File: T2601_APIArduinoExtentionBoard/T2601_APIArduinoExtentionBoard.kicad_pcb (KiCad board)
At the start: 4 copper layers, 59.8 x 90 mm, 100 parts, among them J1 Conn_01x10_Socket, J10 Conn_02x03_Counter_Clockwise, J11 Conn_01x04, J12 Screw_Terminal_01x02, J14 Screw_Terminal_01x02, J2 Conn_01x10_Socket, J20 Conn_02x08_Counter_Clockwise, J21 Conn_02x08_Counter_Clockwise, J3 Conn_01x10_Socket, J30 Conn_01x04_Pin, J31 Conn_01x04_Pin, J4 Conn_01x10_Socket, J5 Screw_Terminal_01x08, J6 Screw_Terminal_01x08, U2 ATmega328PB-A, X1 X322516MOB4SI

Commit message: Reorganisation schematic
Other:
- board text added: "T2601 APIArduino V1.0 Extention JGY & DDP"
- board text removed: "T2601 APIArduino V1 Extention JGY & DDP"
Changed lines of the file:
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@@
 		)
 	)
-	(gr_text "T2601 APIArduino\nV1 Extention\nJGY & DDP"
+	(gr_text "T2601 APIArduino\nV1.0 Extention\nJGY & DDP"
 		(at 153.434 105.534 0)
 		(layer "F.SilkS")
@@
 	)
 	(segment
+		(start 129.6416 114.4778)
+		(end 129.6416 109.6264)
+		(width 1)
+		(layer "F.Cu")
+		(net "Net-(J4-Pin_10)")
+	)
+	(segment
+		(start 129.6416 109.6264)
+		(end 130.81 108.458)
+		(width 1)
+		(layer "F.Cu")
+		(net "Net-(J4-Pin_10)")
+	)
+	(segment
+		(start 132.1816 109.6264)
+		(end 133.35 108.458)
+		(width 1)
+		(layer "F.Cu")
+		(net "Net-(J4-Pin_9)")
+	)
+	(segment
+		(start 132.1816 114.4778)
+		(end 132.1816 109.6264)
+		(width 1)
+		(layer "F.Cu")
+		(net "Net-(J4-Pin_9)")
+	)
+	(segment
+		(start 134.7216 109.626399)
+		(end 135.889999 108.458)
+		(width 1)
+		(layer "F.Cu")
+		(net "Net-(J4-Pin_8)")
+	)
+	(segment
+		(start 134.7216 114.4778)
+		(end 134.7216 109.626399)
+		(width 1)
+		(layer "F.Cu")
+		(net "Net-(J4-Pin_8)")
+	)
+	(segment
+		(start 137.2616 114.4778)
+		(end 137.2616 109.6264)
+		(width 1)
+		(layer "F.Cu")
+		(net "Net-(J4-Pin_7)")
+	)
+	(segment
+		(start 137.2616 109.6264)
+		(end 138.43 108.458)
+		(width 1)
+		(layer "F.Cu")
+		(net "Net-(J4-Pin_7)")
+	)
+	(segment
+		(start 146.05 108.458)
+		(end 145.796 108.458)
+		(width 1)
+		(layer "F.Cu")
+		(net "Net-(J4-Pin_4)")
+	)
+	(segment
+		(start 145.8214 108.458)
+		(end 146.05 108.458)
+		(width 1)
+		(layer "F.Cu")
+		(net "Net-(J4-Pin_4)")
+	)
+	(segment
+		(start 139.8016 114.4778)
+		(end 145.8214 108.458)
+		(width 1)
+		(layer "F.Cu")
+		(net "Net-(J4-Pin_4)")
+	)
+	(segment
+		(start 148.3614 108.458)
+		(end 148.590001 108.458)
+		(width 1)
+		(layer "F.Cu")
+		(net "Net-(J4-Pin_3)")
+	)
+	(segment
+		(start 148.590001 108.458)
+		(end 148.336 108.458)
+		(width 1)
+		(layer "F.Cu")
+		(net "Net-(J4-Pin_3)")
+	)
+	(segment
+		(start 142.3416 114.4778)
+		(end 148.3614 108.458)
+		(width 1)
+		(layer "F.Cu")
+		(net "Net-(J4-Pin_3)")
+	)
+	(segment
+		(start 151.13 108.458)
+		(end 150.876 108.458)
+		(width 1)
+		(layer "F.Cu")
+		(net "Net-(J4-Pin_2)")
+	)
+	(segment
+		(start 144.8816 114.4778)
+		(end 150.9014 108.458)
+		(width 1)
+		(layer "F.Cu")
+		(net "Net-(J4-Pin_2)")
+	)
+	(segment
+		(start 150.9014 108.458)
+		(end 151.13 108.458)
+		(width 1)
+		(layer "F.Cu")
+		(net "Net-(J4-Pin_2)")
+	)
+	(segment
+		(start 153.67 108.458)
+		(end 153.416 108.458)
+		(width 1)
+		(layer "F.Cu")
+		(net "Net-(J4-Pin_1)")
+	)
+	(segment
+		(start 147.4216 114.4778)
+		(end 147.6502 114.4778)
+		(width 1)
+		(layer "F.Cu")
+		(net "Net-(J4-Pin_1)")
+	)
+	(segment
+		(start 147.6502 114.4778)
+		(end 153.67 108.458)
+		(width 1)
+		(layer "F.Cu")
+		(net "Net-(J4-Pin_1)")
+	)
+	(segment
 		(start 130.7592 70.1256)
 		(end 135.36 65.5248)
@@
 		(net "Net-(D12-Pad1)")
 	)
-	(segment
-		(start 134.7216 109.626399)
-		(end 135.889999 108.458)
-		(width 1)
-		(layer "F.Cu")
-		(net "Net-(J4-Pin_8)")
-	)
-	(segment
-		(start 134.7216 114.4778)
-		(end 134.7216 109.626399)
-		(width 1)
-		(layer "F.Cu")
-		(net "Net-(J4-Pin_8)")
-	)
-	(segment
-		(start 129.6416 114.4778)
-		(end 129.6416 109.6264)
-		(width 1)
-		(layer "F.Cu")
-		(net "Net-(J4-Pin_10)")
-	)
-	(segment
-		(start 129.6416 109.6264)
-		(end 130.81 108.458)
-		(width 1)
-		(layer "F.Cu")
-		(net "Net-(J4-Pin_10)")
-	)
-	(segment
-		(start 146.05 108.458)
-		(end 145.796 108.458)
-		(width 1)
-		(layer "F.Cu")
-		(net "Net-(J4-Pin_4)")
-	)
-	(segment
-		(start 145.8214 108.458)
-		(end 146.05 108.458)
-		(width 1)
-		(layer "F.Cu")
-		(net "Net-(J4-Pin_4)")
-	)
-	(segment
-		(start 139.8016 114.4778)
-		(end 145.8214 108.458)
-		(width 1)
-		(layer "F.Cu")
-		(net "Net-(J4-Pin_4)")
-	)
-	(segment
-		(start 151.13 108.458)
-		(end 150.876 108.458)
-		(width 1)
-		(layer "F.Cu")
-		(net "Net-(J4-Pin_2)")
-	)
-	(segment
-		(start 144.8816 114.4778)
-		(end 150.9014 108.458)
-		(width 1)
-		(layer "F.Cu")
-		(net "Net-(J4-Pin_2)")
-	)
-	(segment
-		(start 150.9014 108.458)
-		(end 151.13 108.458)
-		(width 1)
-		(layer "F.Cu")
-		(net "Net-(J4-Pin_2)")
-	)
-	(segment
-		(start 137.2616 114.4778)
-		(end 137.2616 109.6264)
-		(width 1)
-		(layer "F.Cu")
-		(net "Net-(J4-Pin_7)")
-	)
-	(segment
-		(start 137.2616 109.6264)
-		(end 138.43 108.458)
-		(width 1)
-		(layer "F.Cu")
-		(net "Net-(J4-Pin_7)")
-	)
-	(segment
-		(start 148.3614 108.458)
-		(end 148.590001 108.458)
-		(width 1)
-		(layer "F.Cu")
-		(net "Net-(J4-Pin_3)")
-	)
-	(segment
-		(start 148.590001 108.458)
-		(end 148.336 108.458)
-		(width 1)
-		(layer "F.Cu")
-		(net "Net-(J4-Pin_3)")
-	)
-	(segment
-		(start 142.3416 114.4778)
-		(end 148.3614 108.458)
-		(width 1)
-		(layer "F.Cu")
-		(net "Net-(J4-Pin_3)")
-	)
-	(segment
-		(start 132.1816 109.6264)
-		(end 133.35 108.458)
-		(width 1)
-		(layer "F.Cu")
-		(net "Net-(J4-Pin_9)")
-	)
-	(segment
-		(start 132.1816 114.4778)
-		(end 132.1816 109.6264)
-		(width 1)
-		(layer "F.Cu")
-		(net "Net-(J4-Pin_9)")
-	)
-	(segment
-		(start 153.67 108.458)
-		(end 153.416 108.458)
-		(width 1)
-		(layer "F.Cu")
-		(net "Net-(J4-Pin_1)")
-	)
-	(segment
-		(start 147.4216 114.4778)
-		(end 147.6502 114.4778)
-		(width 1)
-		(layer "F.Cu")
-		(net "Net-(J4-Pin_1)")
-	)
-	(segment
-		(start 147.6502 114.4778)
-		(end 153.67 108.458)
-		(width 1)
-		(layer "F.Cu")
-		(net "Net-(J4-Pin_1)")
-	)
 	(zone

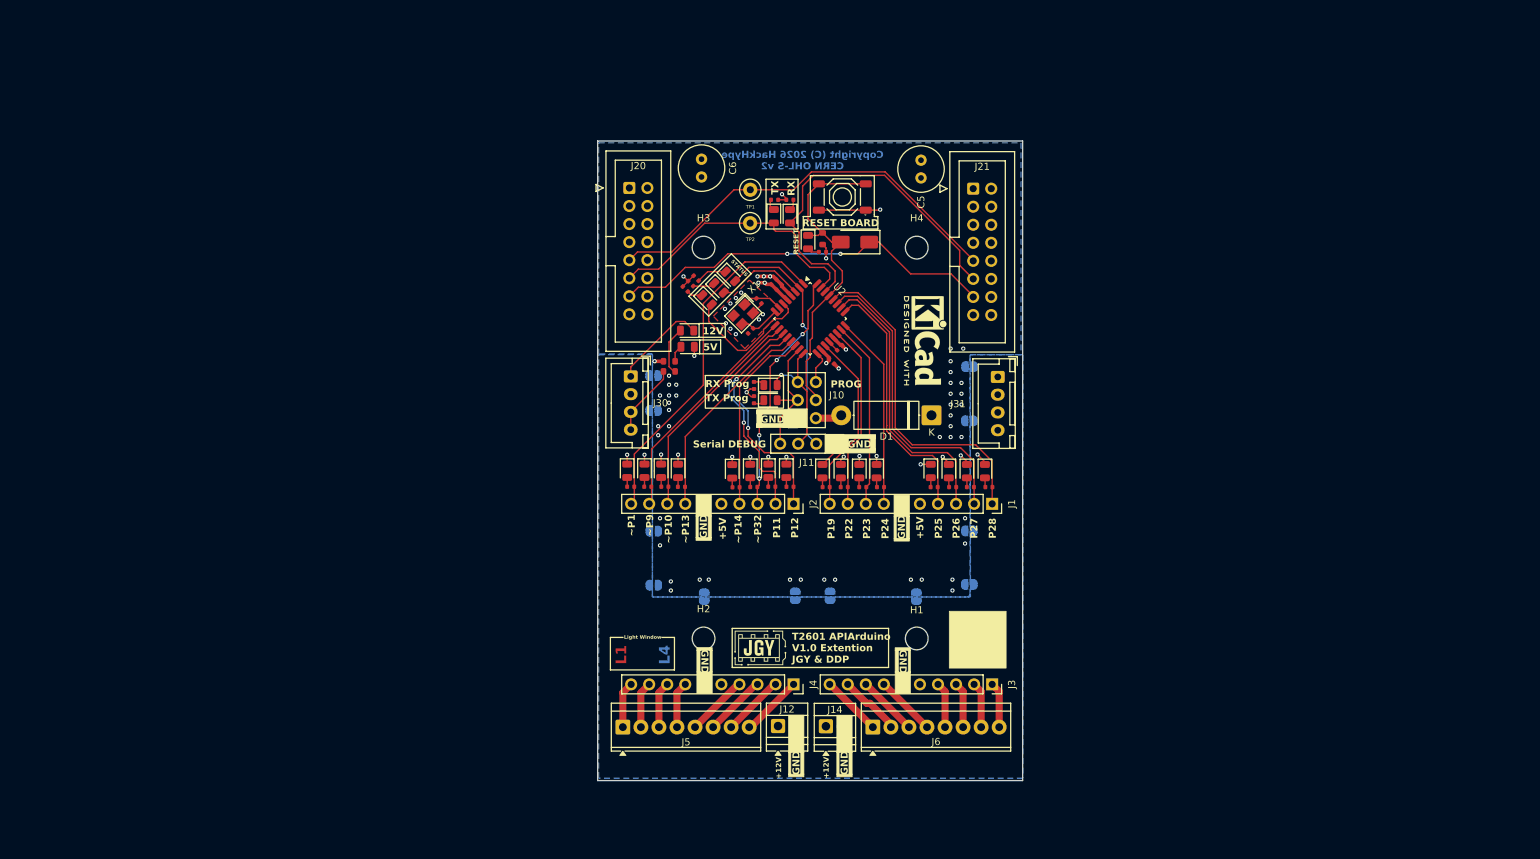
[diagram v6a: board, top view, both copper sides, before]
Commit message: Nouveau schematic selon template V1
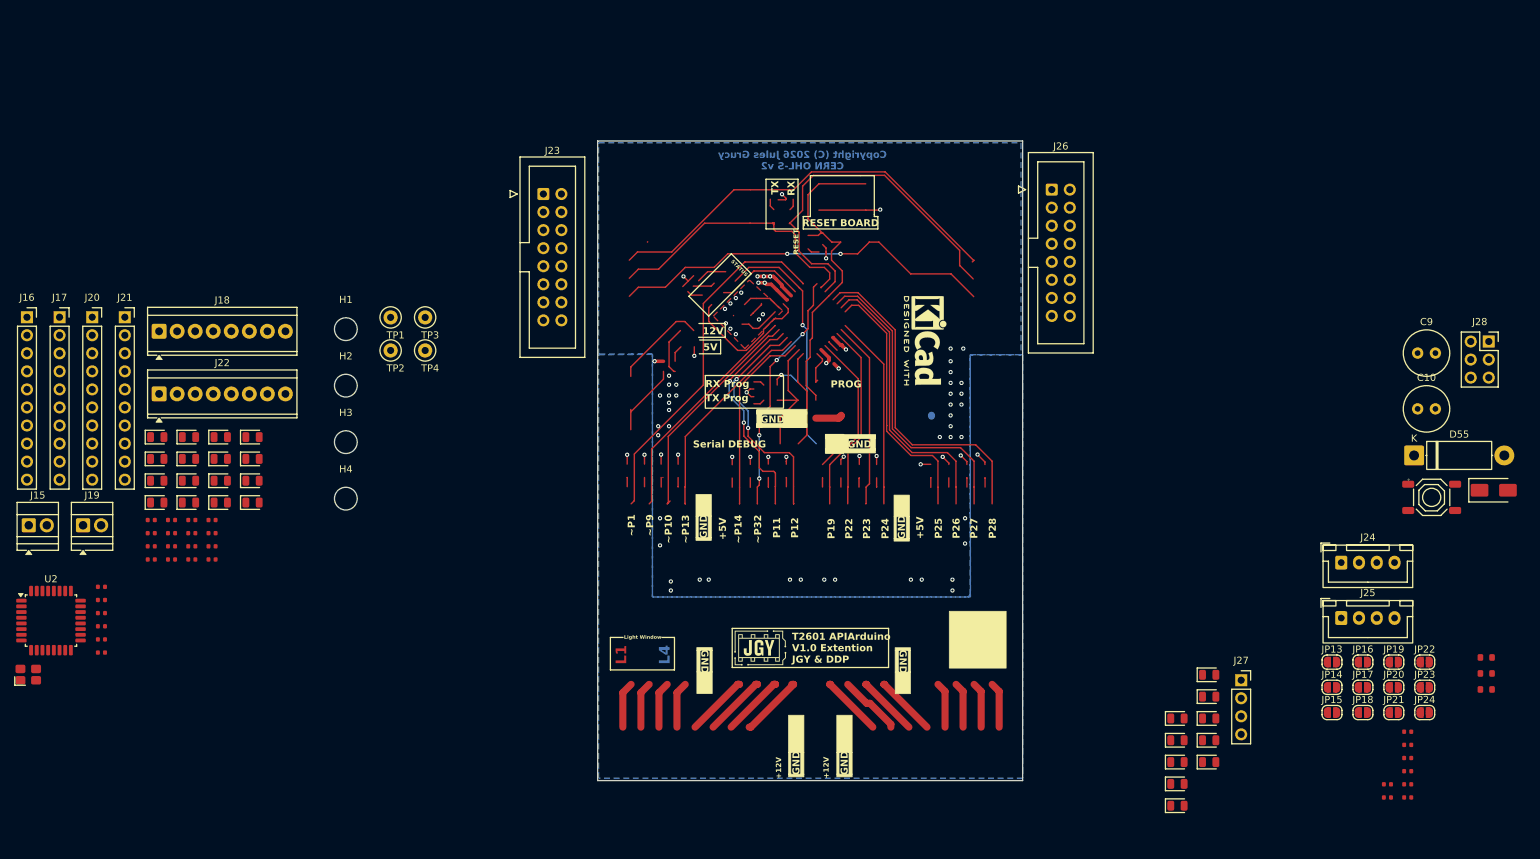
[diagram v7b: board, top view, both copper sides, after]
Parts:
- removed C1, C2: 22pF, PCM_JLCPCB:C_0402
- removed C3, C7, C8: 100nF, PCM_JLCPCB:C_0402
- removed C5, C6: C, Capacitor_THT:C_Radial_D6.3mm_H11.0mm_P2.50mm
- removed D1: D_Schottky, Diode_THT:D_5W_P12.70mm_Horizontal
- removed D10, D11, D12, D9: Yellow, PCM_JLCPCB:D_0805
- removed D14, D15, D16, D17, D18, D19, D2, D20, D21, D22, D23, D24, D25, D28, D3, D4, D5, D7, D8: Green, PCM_JLCPCB:D_0805
- removed D26, D27: Red, PCM_JLCPCB:D_0805
- removed D6: M7, PCM_JLCPCB:D_SMA
- removed J1, J2, J3, J4: Conn_01x10_Socket, Connector_PinSocket_2.54mm:PinSocket_1x10_P2.54mm_Vertical
- removed J10: Conn_02x03_Counter_Clockwise, Connector_PinSocket_2.54mm:PinSocket_2x03_P2.54mm_Vertical
- removed J11: Conn_01x04, Connector_PinSocket_2.54mm:PinSocket_1x04_P2.54mm_Vertical
- removed J12, J14: Screw_Terminal_01x02, TerminalBlock:TerminalBlock_Xinya_XY308-2.54-2P_1x02_P2.54mm_Horizontal
- removed J30, J31: Conn_01x04_Pin, Connector_JST:JST_XH_B4B-XH-A_1x04_P2.50mm_Vertical
- removed J5, J6: Screw_Terminal_01x08, TerminalBlock_TE-Connectivity:TerminalBlock_TE_282834-8_1x08_P2.54mm_Horizontal
- removed JP1, JP10, JP11, JP12, JP2, JP3, JP4, JP5, JP6, JP7, JP8, JP9: SolderJumper_2_Open, Jumper:SolderJumper-2_P1.3mm_Open_RoundedPad1.0x1.5mm
- removed R1, R10, R11, R12, R13, R14, R15, R16, R17, R18, R19, R20, R21, R22, R25, R26, R27, R3, R4, R6, R7, R8, R9: 1kΩ, PCM_JLCPCB:R_0402
- removed R23: 2.4kΩ, PCM_JLCPCB:R_0603
- removed R24: 1kΩ, PCM_JLCPCB:R_0603
- removed R5: 5.6kΩ, PCM_JLCPCB:R_0603
- removed S1: Tactile Button, 160gf, PCM_JLCPCB:SW-SMD_4P-L5.1-W5.1-P3.70-LS6.5-TL-2
- removed X1: X322516MOB4SI, T2601_APIArduinoExtentionBoard_Lib:CRYSTAL-SMD_4P-L3.2-W2.5-BL
- added C10: C, Capacitor_THT:C_Radial_D6.3mm_H11.0mm_P2.50mm, F.Cu at (241.5, 69.7)
- added C11: 100nF, PCM_JLCPCB:C_0402, F.Cu at (56.3, 94.7)
- added C12: 100nF, PCM_JLCPCB:C_0402, F.Cu at (56.3, 96.6)
- added C13: 22pF, PCM_JLCPCB:C_0402, F.Cu at (56.3, 98.4)
- added C14: 100nF, PCM_JLCPCB:C_0402, F.Cu at (56.3, 100.3)
- added C15: 100nF, PCM_JLCPCB:C_0402, F.Cu at (56.3, 102.1)
- added C16: 22pF, PCM_JLCPCB:C_0402, F.Cu at (56.3, 104.0)
- added D30: Green, PCM_JLCPCB:D_0805, F.Cu at (64.1, 76.7)
- added D31: Green, PCM_JLCPCB:D_0805, F.Cu at (64.1, 79.8)
- added D32: Green, PCM_JLCPCB:D_0805, F.Cu at (64.1, 82.9)
- added D33: Green, PCM_JLCPCB:D_0805, F.Cu at (68.6, 73.7)
- added D34: Green, PCM_JLCPCB:D_0805, F.Cu at (68.6, 76.7)
- added D35: Green, PCM_JLCPCB:D_0805, F.Cu at (68.6, 79.8)
- added D36: Green, PCM_JLCPCB:D_0805, F.Cu at (68.6, 82.9)
- added D37: Green, PCM_JLCPCB:D_0805, F.Cu at (73.1, 73.7)
- added D38: Green, PCM_JLCPCB:D_0805, F.Cu at (73.1, 76.7)
- added D39: Green, PCM_JLCPCB:D_0805, F.Cu at (73.1, 79.8)
- added D40: Green, PCM_JLCPCB:D_0805, F.Cu at (73.1, 82.9)
- added D41: Green, PCM_JLCPCB:D_0805, F.Cu at (77.5, 73.7)
- added D42: Green, PCM_JLCPCB:D_0805, F.Cu at (77.5, 76.7)
- added D43: Green, PCM_JLCPCB:D_0805, F.Cu at (77.5, 79.8)
- added D44: Green, PCM_JLCPCB:D_0805, F.Cu at (77.5, 82.9)
- added D45: Red, PCM_JLCPCB:D_0805, F.Cu at (207.7, 113.3)
- added D46: Green, PCM_JLCPCB:D_0805, F.Cu at (207.7, 116.3)
- added D47: Yellow, PCM_JLCPCB:D_0805, F.Cu at (207.7, 119.4)
- added D48: Yellow, PCM_JLCPCB:D_0805, F.Cu at (207.7, 122.5)
- added D49: Yellow, PCM_JLCPCB:D_0805, F.Cu at (207.7, 125.5)
- added D50: Green, PCM_JLCPCB:D_0805, F.Cu at (212.2, 107.1)
- added D51: Green, PCM_JLCPCB:D_0805, F.Cu at (212.2, 110.2)
- added D52: Yellow, PCM_JLCPCB:D_0805, F.Cu at (212.2, 113.3)
- added D53: Red, PCM_JLCPCB:D_0805, F.Cu at (212.2, 116.3)
- added D54: Yellow, PCM_JLCPCB:D_0805, F.Cu at (212.2, 119.4)
- added D55: D_Schottky, Diode_THT:D_5W_P12.70mm_Horizontal, F.Cu at (241.0, 76.2)
- added D56: M7, PCM_JLCPCB:D_SMA, F.Cu at (252.2, 81.1)
- added J15: Screw_Terminal_01x02, TerminalBlock:TerminalBlock_Xinya_XY308-2.54-2P_1x02_P2.54mm_Horizontal, F.Cu at (46.0, 86.1)
- added J16: Conn_01x10_Socket, Connector_PinSocket_2.54mm:PinSocket_1x10_P2.54mm_Vertical, F.Cu at (45.8, 56.8)
- added J17: Conn_01x10_Socket, Connector_PinSocket_2.54mm:PinSocket_1x10_P2.54mm_Vertical, F.Cu at (50.4, 56.8)
- added J18: Screw_Terminal_01x08, TerminalBlock_TE-Connectivity:TerminalBlock_TE_282834-8_1x08_P2.54mm_Horizontal, F.Cu at (64.4, 58.8)
- added J19: Screw_Terminal_01x02, TerminalBlock:TerminalBlock_Xinya_XY308-2.54-2P_1x02_P2.54mm_Horizontal, F.Cu at (53.7, 86.1)
- added J22: Screw_Terminal_01x08, TerminalBlock_TE-Connectivity:TerminalBlock_TE_282834-8_1x08_P2.54mm_Horizontal, F.Cu at (64.4, 67.6)
- added J23: Conn_02x08_Counter_Clockwise, Connector_IDC:IDC-Header_2x08_P2.54mm_Vertical, F.Cu at (118.5, 39.5)
- added J24: Conn_01x04_Pin, Connector_JST:JST_XH_B4B-XH-A_1x04_P2.50mm_Vertical, F.Cu at (230.7, 91.3)
- added J25: Conn_01x04_Pin, Connector_JST:JST_XH_B4B-XH-A_1x04_P2.50mm_Vertical, F.Cu at (230.7, 99.1)
- added J26: Conn_02x08_Counter_Clockwise, Connector_IDC:IDC-Header_2x08_P2.54mm_Vertical, F.Cu at (190.0, 38.8)
- added J27: Conn_01x04, Connector_PinSocket_2.54mm:PinSocket_1x04_P2.54mm_Vertical, F.Cu at (216.7, 107.9)
- added J28: Conn_02x03_Counter_Clockwise, Connector_PinSocket_2.54mm:PinSocket_2x03_P2.54mm_Vertical, F.Cu at (251.5, 60.2)
- added JP13: SolderJumper_2_Open, Jumper:SolderJumper-2_P1.3mm_Open_RoundedPad1.0x1.5mm, F.Cu at (229.4, 105.3)
- added JP14: SolderJumper_2_Open, Jumper:SolderJumper-2_P1.3mm_Open_RoundedPad1.0x1.5mm, F.Cu at (229.4, 108.9)
- added JP15: SolderJumper_2_Open, Jumper:SolderJumper-2_P1.3mm_Open_RoundedPad1.0x1.5mm, F.Cu at (229.4, 112.4)
- added JP16: SolderJumper_2_Open, Jumper:SolderJumper-2_P1.3mm_Open_RoundedPad1.0x1.5mm, F.Cu at (233.8, 105.3)
- added JP17: SolderJumper_2_Open, Jumper:SolderJumper-2_P1.3mm_Open_RoundedPad1.0x1.5mm, F.Cu at (233.8, 108.9)
- added JP18: SolderJumper_2_Open, Jumper:SolderJumper-2_P1.3mm_Open_RoundedPad1.0x1.5mm, F.Cu at (233.8, 112.4)
- added JP19: SolderJumper_2_Open, Jumper:SolderJumper-2_P1.3mm_Open_RoundedPad1.0x1.5mm, F.Cu at (238.1, 105.3)
- added JP20: SolderJumper_2_Open, Jumper:SolderJumper-2_P1.3mm_Open_RoundedPad1.0x1.5mm, F.Cu at (238.1, 108.9)
- added JP21: SolderJumper_2_Open, Jumper:SolderJumper-2_P1.3mm_Open_RoundedPad1.0x1.5mm, F.Cu at (238.1, 112.4)
- added JP22: SolderJumper_2_Open, Jumper:SolderJumper-2_P1.3mm_Open_RoundedPad1.0x1.5mm, F.Cu at (242.5, 105.3)
- added JP23: SolderJumper_2_Open, Jumper:SolderJumper-2_P1.3mm_Open_RoundedPad1.0x1.5mm, F.Cu at (242.5, 108.9)
- added JP24: SolderJumper_2_Open, Jumper:SolderJumper-2_P1.3mm_Open_RoundedPad1.0x1.5mm, F.Cu at (242.5, 112.4)
- added R29: 1kΩ, PCM_JLCPCB:R_0402, F.Cu at (63.3, 87.2)
- added R30: 1kΩ, PCM_JLCPCB:R_0402, F.Cu at (63.3, 89.0)
- added R31: 1kΩ, PCM_JLCPCB:R_0402, F.Cu at (63.3, 90.9)
- added R32: 1kΩ, PCM_JLCPCB:R_0402, F.Cu at (66.1, 85.3)
- added R33: 1kΩ, PCM_JLCPCB:R_0402, F.Cu at (66.1, 87.2)
- added R34: 1kΩ, PCM_JLCPCB:R_0402, F.Cu at (66.1, 89.0)
- added R35: 1kΩ, PCM_JLCPCB:R_0402, F.Cu at (66.1, 90.9)
- added R36: 1kΩ, PCM_JLCPCB:R_0402, F.Cu at (69.0, 85.3)
- added R37: 1kΩ, PCM_JLCPCB:R_0402, F.Cu at (69.0, 87.2)
- added R38: 1kΩ, PCM_JLCPCB:R_0402, F.Cu at (69.0, 89.0)
- added R39: 1kΩ, PCM_JLCPCB:R_0402, F.Cu at (69.0, 90.9)
- added R40: 1kΩ, PCM_JLCPCB:R_0402, F.Cu at (71.8, 85.3)
- added R41: 1kΩ, PCM_JLCPCB:R_0402, F.Cu at (71.8, 87.2)
- added R42: 1kΩ, PCM_JLCPCB:R_0402, F.Cu at (71.8, 89.0)
- added R43: 1kΩ, PCM_JLCPCB:R_0402, F.Cu at (71.8, 90.9)
- added R44: 1kΩ, PCM_JLCPCB:R_0402, F.Cu at (237.2, 122.5)
- added R45: 1kΩ, PCM_JLCPCB:R_0402, F.Cu at (237.2, 124.4)
- added R46: 1kΩ, PCM_JLCPCB:R_0402, F.Cu at (240.1, 115.1)
- added R47: 1kΩ, PCM_JLCPCB:R_0402, F.Cu at (240.1, 117.0)
- added R48: 1kΩ, PCM_JLCPCB:R_0402, F.Cu at (240.1, 118.8)
- added R49: 2.4kΩ, PCM_JLCPCB:R_0603, F.Cu at (251.1, 104.7)
- added R50: 1kΩ, PCM_JLCPCB:R_0603, F.Cu at (251.1, 106.9)
- added R51: 1kΩ, PCM_JLCPCB:R_0402, F.Cu at (240.1, 120.7)
- added R52: 1kΩ, PCM_JLCPCB:R_0402, F.Cu at (240.1, 122.5)
- added R53: 1kΩ, PCM_JLCPCB:R_0402, F.Cu at (240.1, 124.4)
- added R54: 5.6kΩ, PCM_JLCPCB:R_0603, F.Cu at (251.1, 109.2)
- added S2: Tactile Button, 160gf, PCM_JLCPCB:SW-SMD_4P-L5.1-W5.1-P3.70-LS6.5-TL-2, F.Cu at (243.5, 82.1)
- added TP3: TestPoint, TestPoint:TestPoint_Loop_D2.50mm_Drill1.0mm_LowProfile, F.Cu at (101.8, 56.8)
- added TP4: TestPoint, TestPoint:TestPoint_Loop_D2.50mm_Drill1.0mm_LowProfile, F.Cu at (101.8, 61.5)
- added X2: X322516MOB4SI, PCM_JLCPCB:CRYSTAL-SMD_4P-L3.2-W2.5-BL, F.Cu at (46.0, 107.1)
- C9: value 100nF -> C; footprint PCM_JLCPCB:C_0402 -> Capacitor_THT:C_Radial_D6.3mm_H11.0mm_P2.50mm
- D29: value Yellow -> Green
- J20, J21: value Conn_02x08_Counter_Clockwise -> Conn_01x10_Socket; footprint Connector_IDC:IDC-Header_2x08_P2.54mm_Vertical -> Connector_PinSocket_2.54mm:PinSocket_1x10_P2.54mm_Vertical
- moved J21 120.7 mm to (59.6, 56.8)
- moved U2 115.0 mm to (49.2, 99.5), turned to 0 degrees
- moved H1 91.4 mm to (90.7, 58.5)
- moved H4 87.8 mm to (90.7, 82.3)
- moved R28 81.9 mm to (63.3, 85.3), turned to 0 degrees
- moved C9 81.3 mm to (241.5, 61.8), turned to 0 degrees
- moved D29 79.7 mm to (64.1, 73.7), turned to 0 degrees
- moved J20 77.7 mm to (55.0, 56.8)
- moved H2 61.6 mm to (90.7, 66.4)
- moved H3 57.3 mm to (90.7, 74.4)
- moved TP1 53.7 mm to (97.0, 56.8)
- moved TP2 53.7 mm to (97.0, 61.5)
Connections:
- C9 pad 1: Net-(U2-AREF) -> +5V
- D29 pad 1: Net-(D29-Pad1) -> GND
- D29 pad 2: P6 -> Net-(D29-Pad2)
- J20 pad 1: +5V -> Net-(J20-Pin_1)
- J20 pad 10: GND -> Net-(J20-Pin_10)
- J20 pad 2: +5V -> Net-(J20-Pin_2)
- J20 pad 3: +5V -> Net-(J20-Pin_3)
- J20 pad 4: +5V -> Net-(J20-Pin_4)
- J20 pad 5: GND -> +12V
- J20 pad 6: GND -> GNDPWR
- J20 pad 7: GND -> Net-(J20-Pin_7)
- J20 pad 8: GND -> Net-(J20-Pin_8)
- J20 pad 9: UART_BACK -> Net-(J20-Pin_9)
- J21 pad 1: +5V -> P12
- J21 pad 10: GND -> P1
- J21 pad 2: +5V -> P11
- J21 pad 3: +5V -> P32
- J21 pad 4: +5V -> P14
- J21 pad 5: GND -> +5V
- J21 pad 7: GND -> P13
- J21 pad 8: GND -> P10
- J21 pad 9: UART_BACK -> P9
- R28 pad 1: Net-(D29-Pad1) -> P19
- R28 pad 2: GND -> Net-(D29-Pad2)
- TP1 pad 1: UART_BACK -> TX
- TP2 pad 1: TX -> UART_BACK
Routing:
- net (no net): track 0.00 -> 174.9 mm
- net P1: track 50.2 -> 0.00 mm
- net GND: track 51.9 -> 102.2 mm
- net Net-(J4-Pin_3): track 9.00 -> 0.00 mm
- net Net-(J4-Pin_4): track 9.00 -> 0.00 mm
- net Net-(J4-Pin_2): track 9.00 -> 0.00 mm
- net Net-(J4-Pin_1): track 9.00 -> 0.00 mm
- net Net-(J3-Pin_9): track 8.81 -> 0.00 mm
- net Net-(J3-Pin_8): track 8.69 -> 0.00 mm
- net Net-(J3-Pin_10): track 8.69 -> 0.00 mm
- net Net-(J3-Pin_7): track 8.69 -> 0.00 mm
- net Net-(D7-Pad2): track 6.88 -> 0.00 mm
- net Net-(J4-Pin_7): track 6.50 -> 0.00 mm
- net Net-(J4-Pin_9): track 6.50 -> 0.00 mm
- net Net-(J4-Pin_10): track 6.50 -> 0.00 mm
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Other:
- board text added: "Copyright (C) 2026 Jules Grucy CERN OHL-S v2"
- board text removed: "Copyright (C) 2026 HackHype CERN OHL-S v2"

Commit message: Rerouting en cours
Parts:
- removed C15: 100nF, PCM_JLCPCB:C_0402
- removed REF**: KiCad-Logo2_5mm_SilkScreen, Symbol:KiCad-Logo2_5mm_SilkScreen
- added TP5: TestPoint, TestPoint:TestPoint_Loop_D2.50mm_Drill1.0mm_LowProfile, F.Cu at (234.8, 65.2)
- moved J16 164.4 mm to (198.4, 117.8), turned to -90 degrees
- moved J17 153.9 mm to (197.7, 101.3), turned to -90 degrees
- moved J18 134.2 mm to (180.1, 126.7)
- moved JP13 130.7 mm to (98.9, 99.2)
- moved JP14 130.7 mm to (98.9, 102.7)
- moved JP15 130.7 mm to (98.9, 106.3)
- moved JP16 130.7 mm to (103.3, 99.2)
- moved JP17 130.7 mm to (103.3, 102.7)
- moved JP18 130.7 mm to (103.3, 106.3)
- moved JP19 130.7 mm to (107.6, 99.2)
- moved JP20 130.7 mm to (107.6, 102.7)
- moved JP21 130.7 mm to (107.6, 106.3)
- moved JP22 130.7 mm to (112.0, 99.2)
- moved JP23 130.7 mm to (112.0, 102.7)
- moved JP24 130.7 mm to (112.0, 106.3)
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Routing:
- net (no net): track 174.9 -> 0.00 mm
- net GND: track 102.2 -> 4.98 mm, vias 75 -> 0
- net GEN_RESET: track 54.8 -> 0.00 mm, vias 2 -> 0
- net P28: track 46.7 -> 0.00 mm
- net RESET: track 46.4 -> 0.00 mm
- net P27: track 43.4 -> 0.00 mm
- net P26: track 40.1 -> 0.00 mm
- net P25: track 36.6 -> 0.00 mm
- net P32: track 34.5 -> 0.00 mm, vias 4 -> 0
- net P2: track 34.0 -> 0.00 mm, vias 1 -> 0
- net P12: track 32.9 -> 0.00 mm, vias 2 -> 0
- net P9: track 32.4 -> 0.00 mm
- net P10: track 31.9 -> 0.00 mm
- net P11: track 31.3 -> 0.36 mm, vias 2 -> 0
- net P13: track 30.0 -> 0.00 mm
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- removed copper zone on In2.Cu, net +12V
- removed copper zone on In2.Cu, net +5V
- removed copper zone on B.Cu, net GND
- removed copper zone on F.Cu, net GND
- removed copper zone on In1.Cu, net GND
- removed copper zone on B.Cu, net GNDPWR
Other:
- outline, holes or cut-outs redrawn
- board text added: "Copyright (C) 2026 Jules Grucy & Damien de Pascal CERN OHL-S v2"
- board text removed: "+12V"
- board text removed: "+5V"
- board text removed: "12V"
- board text removed: "5V"
- board text removed: "Copyright (C) 2026 Jules Grucy CERN OHL-S v2"
- board text removed: "P11"
- board text removed: "P12"
- board text removed: "P19"
- board text removed: "P22"
- board text removed: "P23"
- board text removed: "P24"
- board text removed: "P25"
- board text removed: "P26"
- board text removed: "P27"
- board text removed: "P28"
- board text removed: "PROG"
- board text removed: "RESET"
- board text removed: "RESET BOARD"
- board text removed: "RX"
- board text removed: "RX Prog"
- board text removed: "STATUS"
- board text removed: "Serial DEBUG"
- board text removed: "TX"
- board text removed: "TX Prog"
- board text removed: "~P1"
- board text removed: "~P10"
- board text removed: "~P13"
- board text removed: "~P14"
- board text removed: "~P32"
- board text removed: "~P9"
